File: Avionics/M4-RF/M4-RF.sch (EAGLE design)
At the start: 30 parts, among them J1 132134RP, J2 132134RP, U1 CC1120, U2 CC1190, U3 CC2520, U4 CC2592, U5 INF-PG-LQFP-100-11-7000X7000E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, U6 LDB182G4520C-110, X1 FA-20H32.0000MF20X-K3

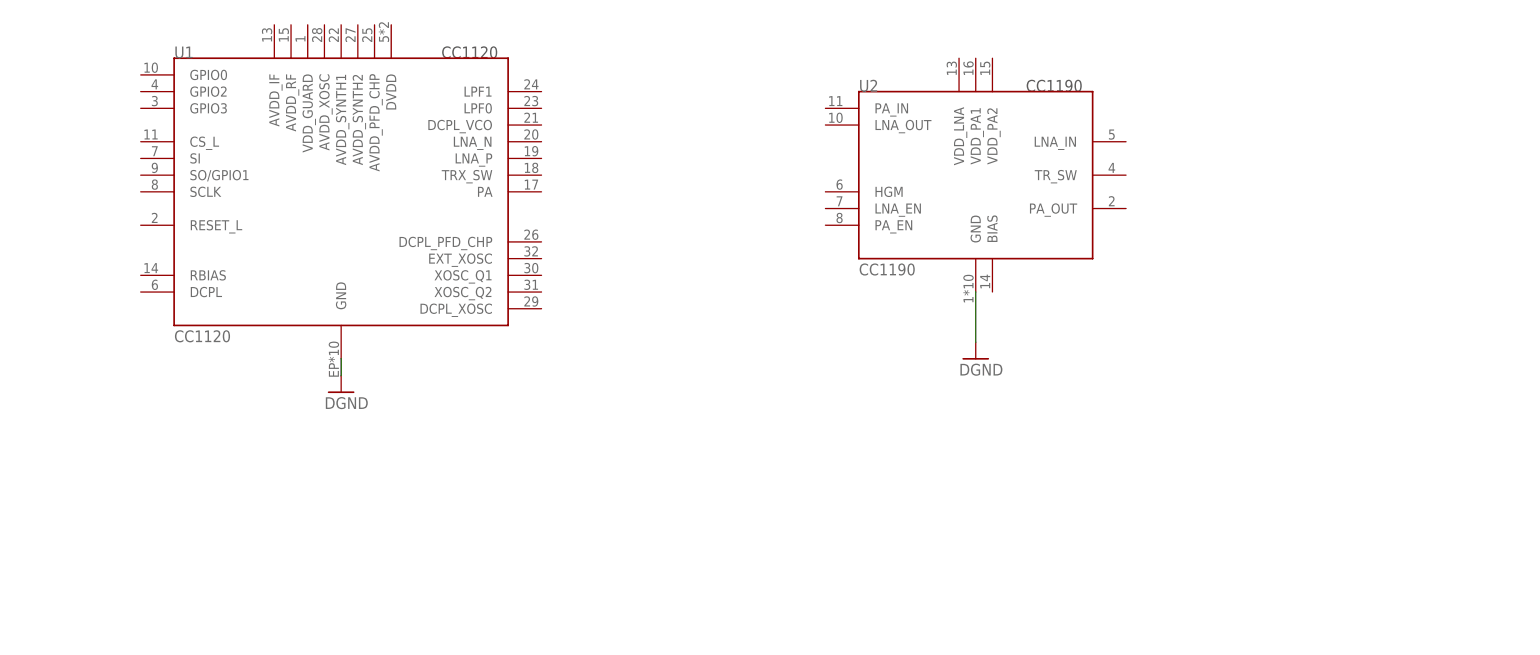
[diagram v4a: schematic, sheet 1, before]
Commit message: Started to build 900MHz circuit
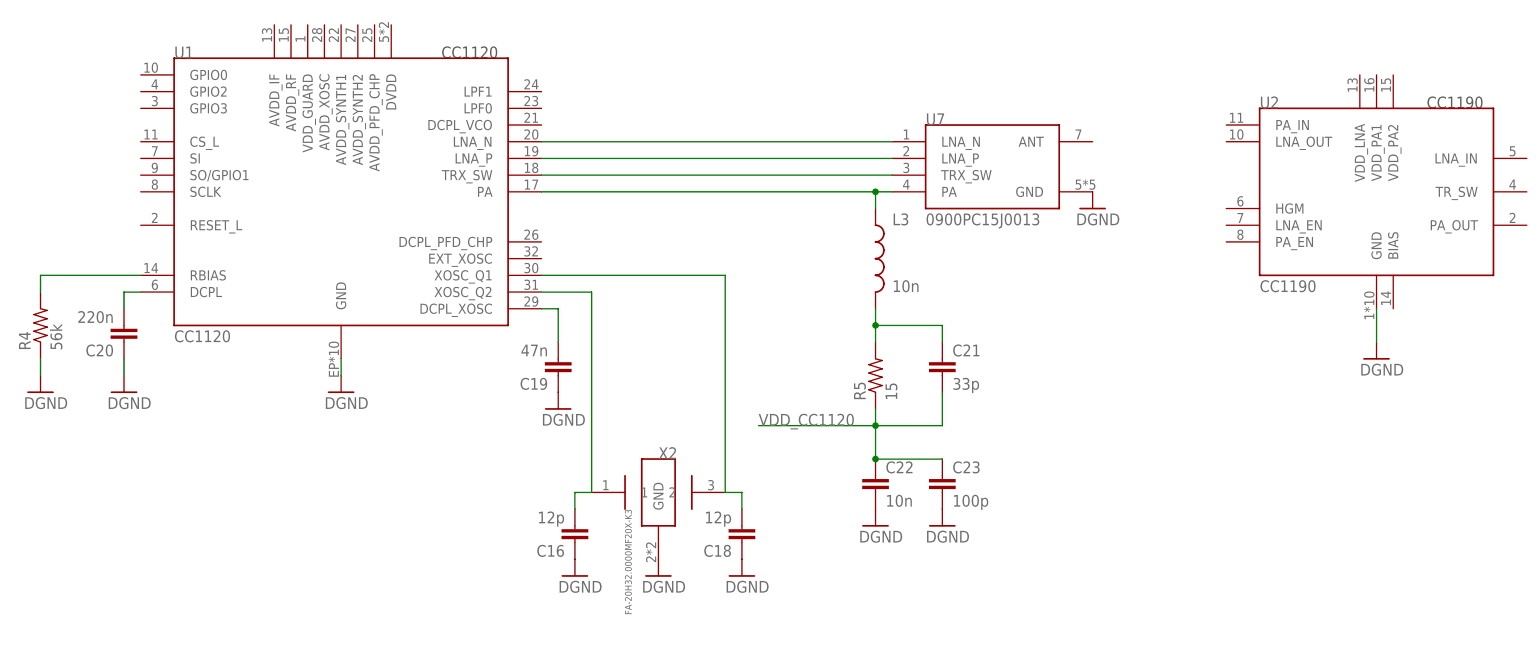
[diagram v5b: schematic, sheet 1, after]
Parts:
- added C12, C13, C14: 0.1u, SparkFun-Capacitors:CAP0402-CAP
- added C15, C17: 2.2u, SparkFun-Capacitors:CAP0402-CAP
- added C16, C18: 12p, SparkFun-Capacitors:CAP0402-CAP
- added C19: 47n, SparkFun-Capacitors:CAP0402-CAP
- added C20: 220n, SparkFun-Capacitors:CAP0402-CAP
- added C21: 33p, SparkFun-Passives:CAP0402-CAP
- added C22: 10n, SparkFun-Passives:CAP0402-CAP
- added C23: 100p, SparkFun-Passives:CAP0402-CAP
- added L1, L2: BEAD 100, SparkFun-Passives:INDUCTOR0402
- added L3: 10n, SparkFun-Passives:INDUCTOR0402
- added R4: 56k, SparkFun-Resistors:RESISTOR0402-RES
- added R5: 15, SparkFun-Resistors:RESISTOR0402-RES
- added U7: 0900PC15J0013, rf:0900PC15J0013
- added X2: FA-20H32.0000MF20X-K3, oscillators:FA-20H32.0000MF20X-K3
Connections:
- new net 2G2_SFD: U3.GPIO4
- new net 2G4_CCA: U3.GPIO3
- new net 2G4_CS_L: U3.CS_L
- new net 2G4_FIFO: U3.GPIO1
- new net 2G4_FIFOP: U3.GPIO2
- new net 2G4_HGM: R6.1
- new net 2G4_LNA_EN: R7.1
- new net 2G4_PA_EN: R8.1
- new net 2G4_RESET_L: U3.RESET_L
- new net 2G4_SCLK: U3.SCLK
- new net 2G4_SI: U3.SI
- new net 2G4_SO: U3.SO
- new net 2G4_VREG_EN: U3.VREG_EN
- new net N$24: C16.2, U1.XOSC_Q2, X2.1
- new net N$25: C18.2, U1.XOSC_Q1, X2.2
- new net N$26: C19.2, U1.DCPL_XOSC
- new net N$27: C20.2, U1.DCPL
- new net N$28: R4.2, U1.RBIAS
- new net N$29: U1.LNA_N, U7.LNA_N
- new net N$30: U1.LNA_P, U7.LNA_P
- new net N$31: U1.TRX_SW, U7.TRX_SW
- new net N$32: L3.1, U1.PA, U7.PA
- new net N$33: C21.1, L3.2, R5.2
- new net VDD_CC1120: C21.2, C22.1, C23.1, R5.1
- new net VDD_CC2520: L1.2
- new net VDD_CC2592: L2.2
- net GND: now also C12.1, C13.1, C14.1, C15.1, C16.1, C17.1, C18.1, C19.1, C20.1, C22.2, C23.2, R4.1, U7.GND, X2.GND
- net N$10: now also C17.2, L2.1
- net N$14: now also C12.2, C13.2, C14.2, C15.2, L1.1
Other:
- moved on the sheet: U2
